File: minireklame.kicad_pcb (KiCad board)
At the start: 2 copper layers, 100 x 50 mm, 62 parts, among them IC1 ATXMEGA64A4U-A, P1 CONN_01X04, P10 CONN_01X04, P11 CONN_01X04, P12 CONN_01X04, P13 CONN_01X04, P14 CONN_01X04, P15 CONN_01X04, P16 CONN_01X04, P17 Screw_Terminal_1x02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

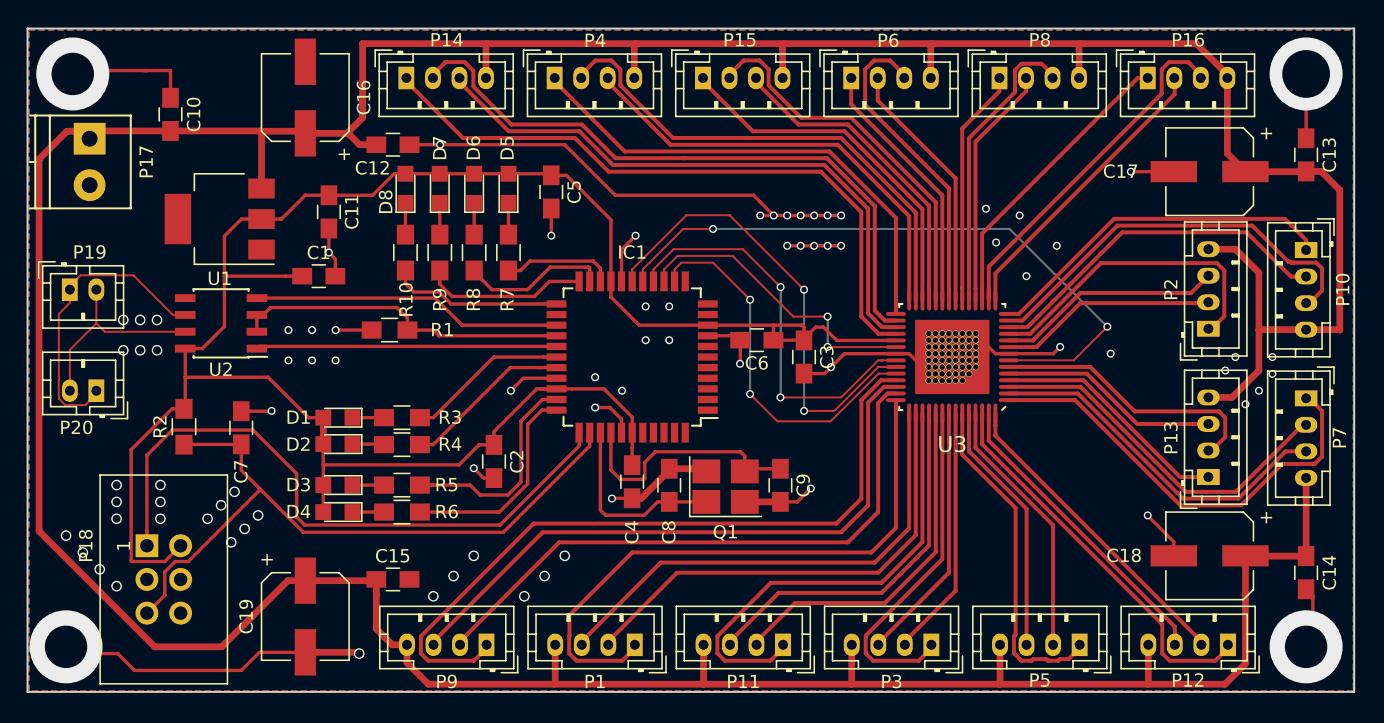
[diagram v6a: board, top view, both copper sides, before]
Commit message: placing vias again as footprint to avoid loss of net information and optimising part numbers on silk
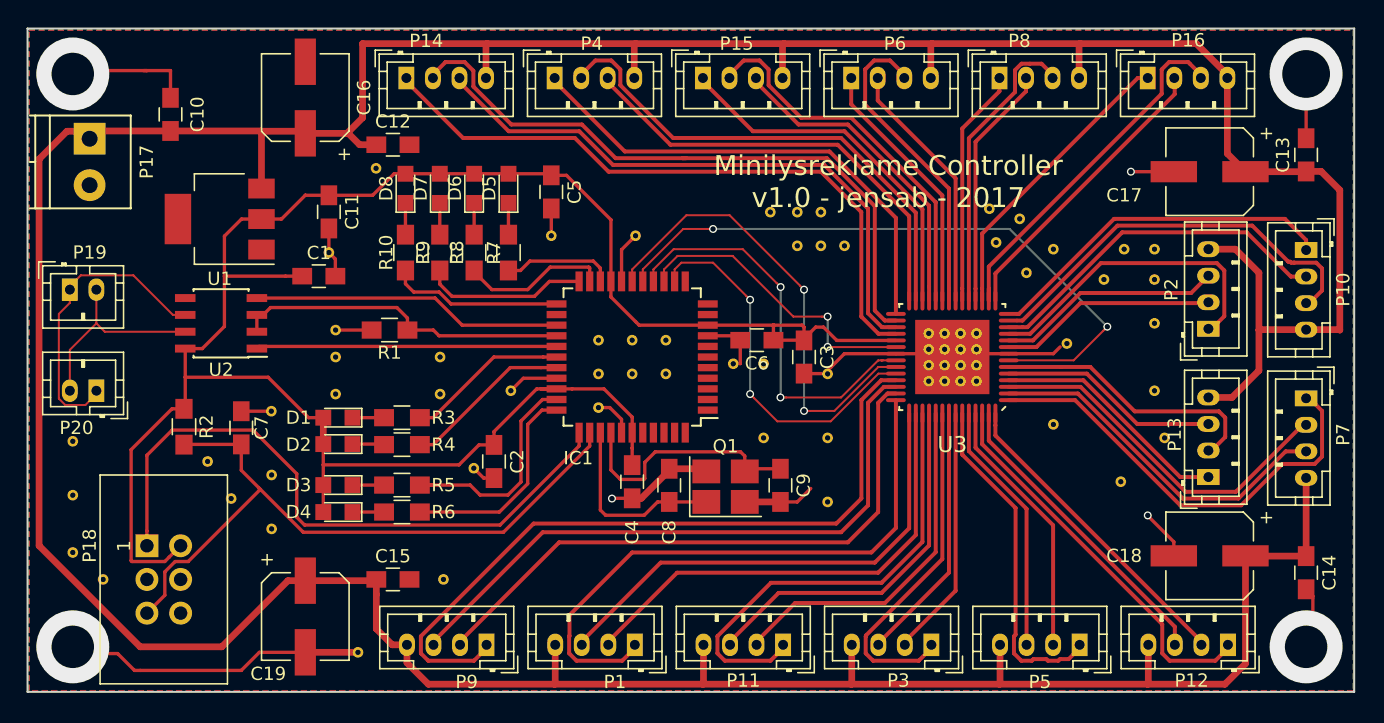
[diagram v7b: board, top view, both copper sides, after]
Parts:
- added REF**: Via-0.8mm, vias:Via-0.8mm, F.Cu at (83.6, 82.6)
- added REF**: Via-0.8mm, vias:Via-0.8mm, F.Cu at (101.1, 77.6)
- added REF**: Via-0.8mm, vias:Via-0.8mm, F.Cu at (101.1, 74.8)
- added REF**: Via-0.8mm, vias:Via-0.8mm, F.Cu at (93.2, 74.8)
- added REF**: Via-0.8mm, vias:Via-0.8mm, F.Cu at (96.3, 60.5)
- added REF**: Via-0.8mm, vias:Via-0.8mm, F.Cu at (141.5, 76.6)
- added REF**: Via-0.8mm, vias:Via-0.8mm, F.Cu at (140.3, 76.6)
- added REF**: Via-0.8mm, vias:Via-0.8mm, F.Cu at (139.1, 76.6)
- added REF**: Via-0.8mm, vias:Via-0.8mm, F.Cu at (137.9, 76.6)
- added REF**: Via-0.8mm, vias:Via-0.8mm, F.Cu at (141.5, 75.4)
- added REF**: Via-0.8mm, vias:Via-0.8mm, F.Cu at (140.3, 75.4)
- added REF**: Via-0.8mm, vias:Via-0.8mm, F.Cu at (85.3, 85.4)
- added REF**: Via-0.8mm, vias:Via-0.8mm, F.Cu at (139.1, 75.4)
- added REF**: Via-0.8mm, vias:Via-0.8mm, F.Cu at (137.9, 75.4)
- added REF**: Via-0.8mm, vias:Via-0.8mm, F.Cu at (141.5, 74.2)
- added REF**: Via-0.8mm, vias:Via-0.8mm, F.Cu at (140.3, 74.2)
- added REF**: Via-0.8mm, vias:Via-0.8mm, F.Cu at (139.1, 74.2)
- added REF**: Via-0.8mm, vias:Via-0.8mm, F.Cu at (137.9, 74.2)
- added REF**: Via-0.8mm, vias:Via-0.8mm, F.Cu at (141.5, 73.0)
- added REF**: Via-0.8mm, vias:Via-0.8mm, F.Cu at (140.3, 73.0)
- added REF**: Via-0.8mm, vias:Via-0.8mm, F.Cu at (139.1, 73.0)
- added REF**: Via-0.8mm, vias:Via-0.8mm, F.Cu at (137.9, 73.0)
- added REF**: Via-0.8mm, vias:Via-0.8mm, F.Cu at (88.4, 87.7)
- added REF**: Via-0.8mm, vias:Via-0.8mm, F.Cu at (147.3, 66.6)
- added REF**: Via-0.8mm, vias:Via-0.8mm, F.Cu at (145.3, 68.4)
- added REF**: Via-0.8mm, vias:Via-0.8mm, F.Cu at (143.0, 66.1)
- added REF**: Via-0.8mm, vias:Via-0.8mm, F.Cu at (144.8, 64.3)
- added REF**: Via-0.8mm, vias:Via-0.8mm, F.Cu at (142.5, 63.6)
- added REF**: Via-0.8mm, vias:Via-0.8mm, F.Cu at (151.1, 68.9)
- added REF**: Via-0.8mm, vias:Via-0.8mm, F.Cu at (154.9, 68.9)
- added REF**: Via-0.8mm, vias:Via-0.8mm, F.Cu at (154.9, 66.6)
- added REF**: Via-0.8mm, vias:Via-0.8mm, F.Cu at (152.7, 66.6)
- added REF**: Via-0.8mm, vias:Via-0.8mm, F.Cu at (154.9, 72.2)
- added REF**: Via-0.8mm, vias:Via-0.8mm, F.Cu at (88.4, 83.7)
- added REF**: Via-0.8mm, vias:Via-0.8mm, F.Cu at (154.9, 77.3)
- added REF**: Via-0.8mm, vias:Via-0.8mm, F.Cu at (155.7, 80.9)
- added REF**: Via-0.8mm, vias:Via-0.8mm, F.Cu at (152.4, 84.2)
- added REF**: Via-0.8mm, vias:Via-0.8mm, F.Cu at (147.3, 79.8)
- added REF**: Via-0.8mm, vias:Via-0.8mm, F.Cu at (131.6, 66.4)
- added REF**: Via-0.8mm, vias:Via-0.8mm, F.Cu at (129.8, 66.4)
- added REF**: Via-0.8mm, vias:Via-0.8mm, F.Cu at (128.0, 66.4)
- added REF**: Via-0.8mm, vias:Via-0.8mm, F.Cu at (128.0, 63.8)
- added REF**: Via-0.8mm, vias:Via-0.8mm, F.Cu at (129.8, 63.8)
- added REF**: Via-0.8mm, vias:Via-0.8mm, F.Cu at (126.0, 63.8)
- added REF**: Via-0.8mm, vias:Via-0.8mm, F.Cu at (73.4, 81.1)
- added REF**: Via-0.8mm, vias:Via-0.8mm, F.Cu at (113.0, 76.0)
- added REF**: Via-0.8mm, vias:Via-0.8mm, F.Cu at (115.6, 76.0)
- added REF**: Via-0.8mm, vias:Via-0.8mm, F.Cu at (118.1, 76.0)
- added REF**: Via-0.8mm, vias:Via-0.8mm, F.Cu at (118.1, 73.5)
- added REF**: Via-0.8mm, vias:Via-0.8mm, F.Cu at (115.6, 73.5)
- added REF**: Via-0.8mm, vias:Via-0.8mm, F.Cu at (113.0, 73.5)
- added REF**: Via-0.8mm, vias:Via-0.8mm, F.Cu at (113.0, 78.6)
- added REF**: Via-0.8mm, vias:Via-0.8mm, F.Cu at (115.8, 65.6)
- added REF**: Via-0.8mm, vias:Via-0.8mm, F.Cu at (109.5, 65.6)
- added REF**: Via-0.8mm, vias:Via-0.8mm, F.Cu at (92.7, 66.9)
- added REF**: Via-0.8mm, vias:Via-0.8mm, F.Cu at (73.4, 85.2)
- added REF**: Via-0.8mm, vias:Via-0.8mm, F.Cu at (93.2, 72.7)
- added REF**: Via-0.8mm, vias:Via-0.8mm, F.Cu at (88.4, 78.8)
- added REF**: Via-0.8mm, vias:Via-0.8mm, F.Cu at (106.4, 77.3)
- added REF**: Via-0.8mm, vias:Via-0.8mm, F.Cu at (103.6, 83.1)
- added REF**: Via-0.8mm, vias:Via-0.8mm, F.Cu at (94.9, 97.0)
- added REF**: Via-0.8mm, vias:Via-0.8mm, F.Cu at (101.4, 91.5)
- added REF**: Via-0.8mm, vias:Via-0.8mm, F.Cu at (123.2, 75.3)
- added REF**: Via-0.8mm, vias:Via-0.8mm, F.Cu at (125.5, 75.3)
- added REF**: Via-0.8mm, vias:Via-0.8mm, F.Cu at (130.3, 76.0)
- added REF**: Via-0.8mm, vias:Via-0.8mm, F.Cu at (130.3, 80.9)
- added REF**: Via-0.8mm, vias:Via-0.8mm, F.Cu at (75.7, 91.5)
- added REF**: Via-0.8mm, vias:Via-0.8mm, F.Cu at (125.5, 80.9)
- added REF**: Via-0.8mm, vias:Via-0.8mm, F.Cu at (130.3, 85.7)
- added REF**: Via-0.8mm, vias:Via-0.8mm, F.Cu at (148.3, 73.7)
- added REF**: Via-0.8mm, vias:Via-0.8mm, F.Cu at (73.4, 89.5)
- added REF**: Via-0.8mm, vias:Via-0.8mm, F.Cu at (93.2, 77.6)
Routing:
- net GND: track 163.5 -> 111.9 mm, vias 84 -> 7
- net +5V: track 331.5 -> 332.2 mm
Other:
- board text added: "Minilysreklame Controller v1.0 - jensab - 2017"
